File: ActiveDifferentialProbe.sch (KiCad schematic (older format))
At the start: 46 parts, among them J1 Conn_01x01, J16 Conn_01x01, J18 Conn_01x01, J19 Conn_01x01, J2 Conn_01x01, J20 Conn_01x01, J21 Conn_01x01, J22 Conn_01x01, J23 Conn_01x01, J25 Conn_Coaxial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

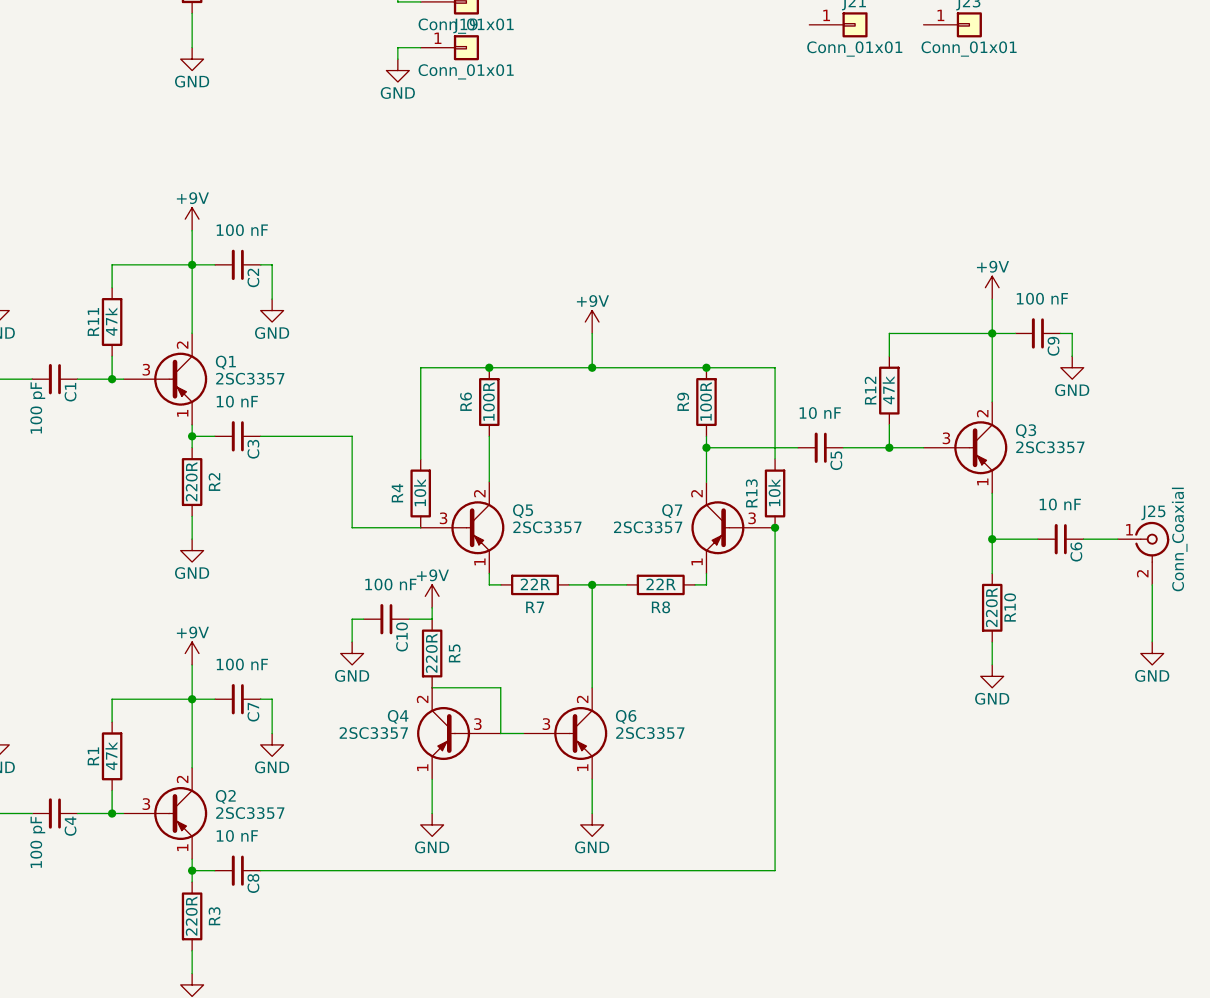
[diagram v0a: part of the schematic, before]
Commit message: Added LCSC parts, fixed symbol, added decoupling resistors
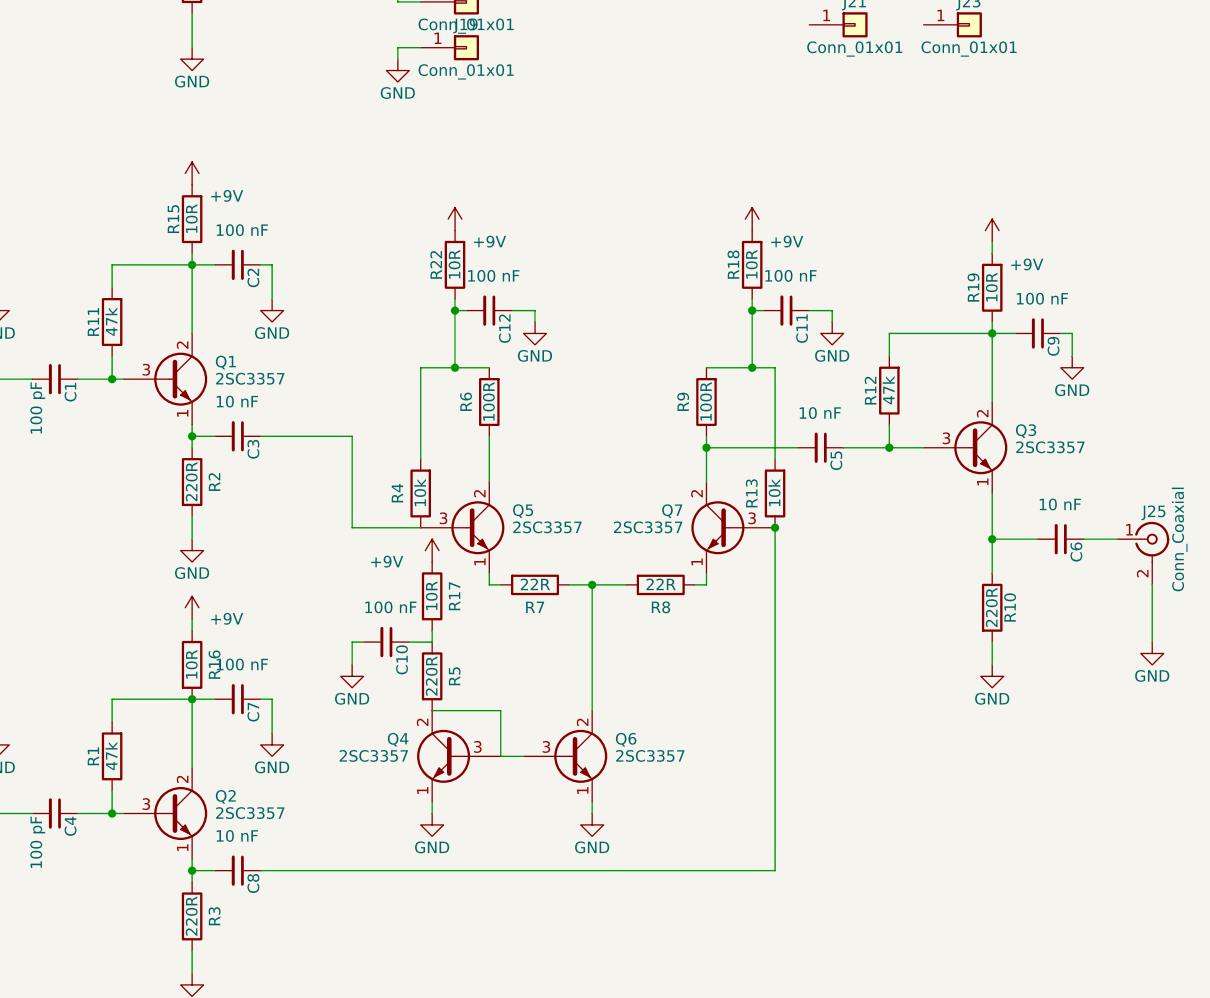
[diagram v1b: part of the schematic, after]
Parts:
- removed Q1, Q2, Q3, Q4, Q5, Q6, Q7: 2SC3357, TO_SOT_Packages_SMD:SOT-89-3_Handsoldering, symbol 2SA1015
- added C11, C12: 100 nF, Capacitors_SMD:C_0805_HandSoldering, symbol C_Small
- added Q1, Q2, Q3, Q4, Q5, Q6, Q7: 2SC3357, TO_SOT_Packages_SMD:SOT-89-3_Handsoldering, symbol 2SC1815
- added R15, R16, R17, R18, R19, R22: 10R, Resistors_SMD:R_0805_HandSoldering, symbol R
- C1, C4: LCSC (none) -> C1790
- C10, C2, C7, C9: LCSC (none) -> C49678
- C16: footprint Capacitors_SMD:C_1210_HandSoldering -> Capacitors_SMD:C_0805_HandSoldering; LCSC (none) -> C45783
- C3, C5, C6, C8: LCSC (none) -> C1710
- D6: LCSC (none) -> C2296
- R1, R11, R12: LCSC (none) -> C17713
- R10, R2, R3, R5: LCSC (none) -> C17557
- R13, R4: LCSC (none) -> C17414
- R14: LCSC (none) -> C17513
- R6, R9: LCSC (none) -> C17408
- R7, R8: LCSC (none) -> C17561
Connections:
- net +9V: now also R15.2, R16.1, R17.1, R18.2, R19.2, R22.2; no longer C10.1, C2.2, C7.2, C9.2, R1.2, R11.2, R12.2, R13.2, R4.2, R5.1, R6.2, R9.2
- net GND: now also C11.1, C12.1, Q4.1 (E), Q6.1 (E)
- net at C1.1, R11.1: now also Q1.3 (B)
- net at C3.2, R2.1: now also Q1.1 (E)
- net at C3.1, R4.1: now also Q5.3 (B)
- net at C5.1, R12.1: now also Q3.3 (B)
- net at C5.2, R9.1: now also Q7.2 (C)
- net at C6.2, R10.1: now also Q3.1 (E)
- net at C4.1, R1.1: now also Q2.3 (B)
- net at C8.2, R3.1: now also Q2.1 (E)
- net at C8.1, R13.1: now also Q7.3 (B)
- net at R5.2: now also Q4.2 (C), Q4.3 (B), Q6.3 (B)
- net at R7.1, R8.2: now also Q6.2 (C)
- net at R7.2: now also Q5.1 (E)
- net at R6.1: now also Q5.2 (C)
- net at R8.1: now also Q7.1 (E)
- new net: C2.2, Q1.2 (C), R11.2, R15.1
- new net: C9.2, Q3.2 (C), R12.2, R19.1
- new net: C7.2, Q2.2 (C), R1.2, R16.2
- new net: C10.1, R17.2, R5.1
- new net: C12.2, R22.1, R4.2, R6.2
- new net: C11.2, R13.2, R18.1, R9.2
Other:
- moved on the sheet: C10, R5

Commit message: Changed to 2SC3356
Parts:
- removed Q1, Q2, Q3, Q4, Q5, Q6, Q7: 2SC3357, TO_SOT_Packages_SMD:SOT-89-3_Handsoldering, symbol 2SC1815
- added Q1, Q2, Q3, Q4, Q5, Q6, Q7: 2SC3356, TO_SOT_Packages_SMD:SOT-23, symbol MMBT3904
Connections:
- net GND: now also Q4.2 (E), Q6.2 (E)
- net at C1.1, R11.1: now also Q1.1 (B)
- net at C3.2, R2.1: now also Q1.2 (E)
- net at C3.1, R4.1: now also Q5.1 (B)
- net at C5.1, R12.1: now also Q3.1 (B)
- net at C5.2, R9.1: now also Q7.3 (C)
- net at C6.2, R10.1: now also Q3.2 (E)
- net at C2.2, R11.2, R15.1: now also Q1.3 (C)
- net at C9.2, R12.2, R19.1: now also Q3.3 (C)
- net at C4.1, R1.1: now also Q2.1 (B)
- net at C8.2, R3.1: now also Q2.2 (E)
- net at C8.1, R13.1: now also Q7.1 (B)
- net at C7.2, R1.2, R16.2: now also Q2.3 (C)
- net at R5.2: now also Q4.1 (B), Q4.3 (C), Q6.1 (B)
- net at R7.1, R8.2: now also Q6.3 (C)
- net at R7.2: now also Q5.2 (E)
- net at R8.1: now also Q7.2 (E)
- net at R6.1: now also Q5.3 (C)

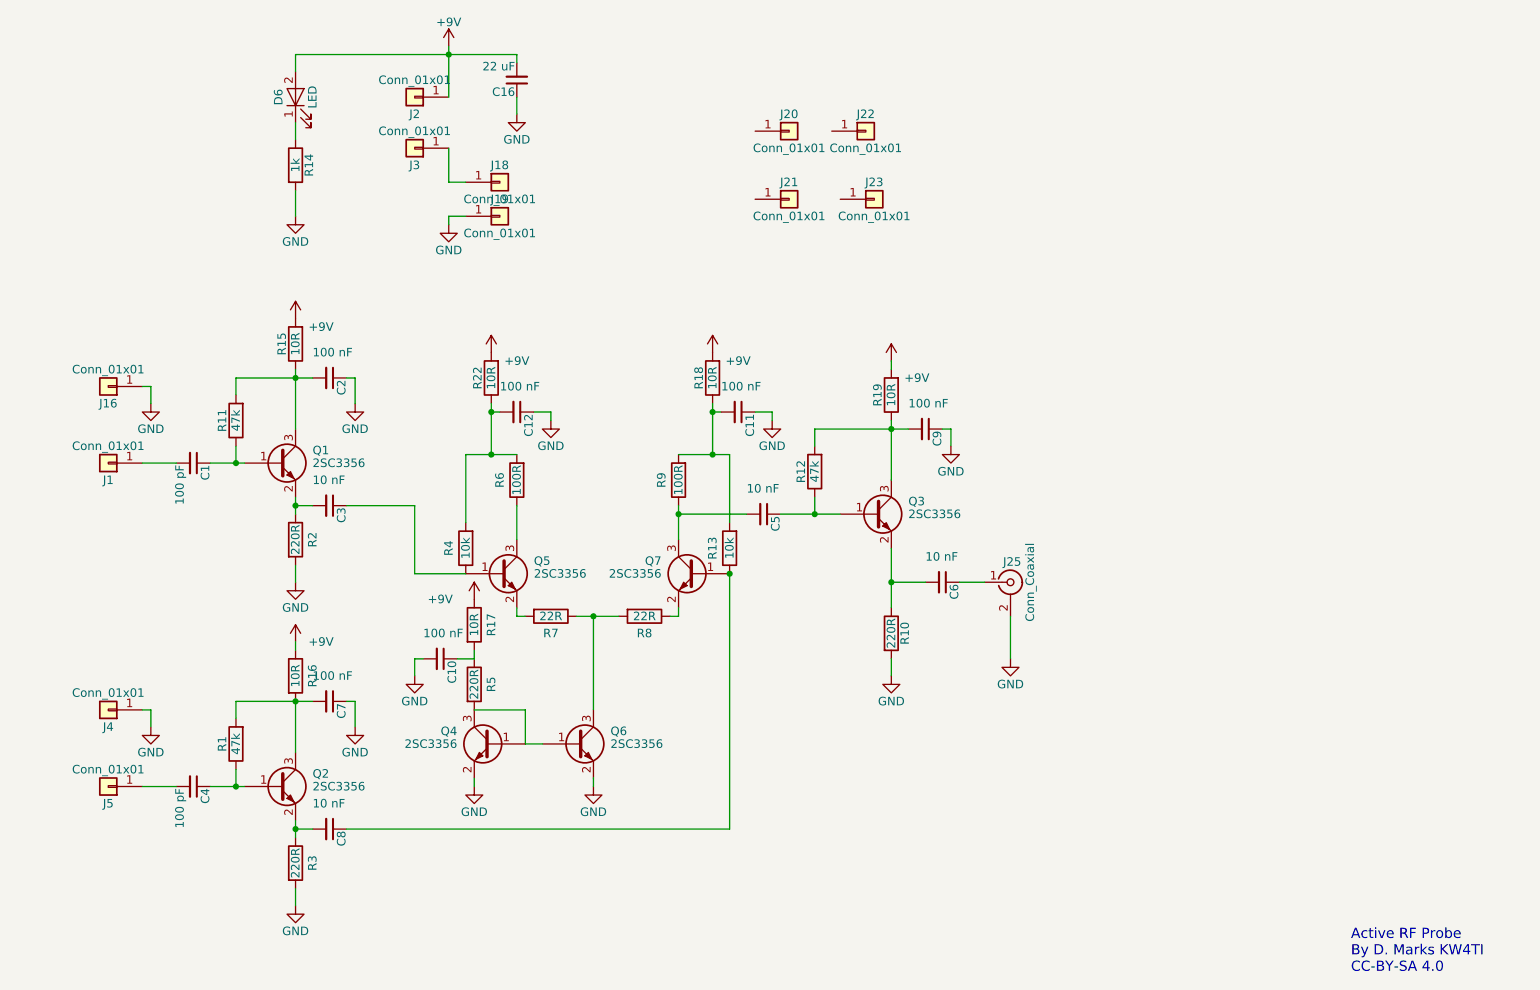
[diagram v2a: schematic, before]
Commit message: Added LCSC part numbers, added cutout notched, added series base resistors to emitter followers
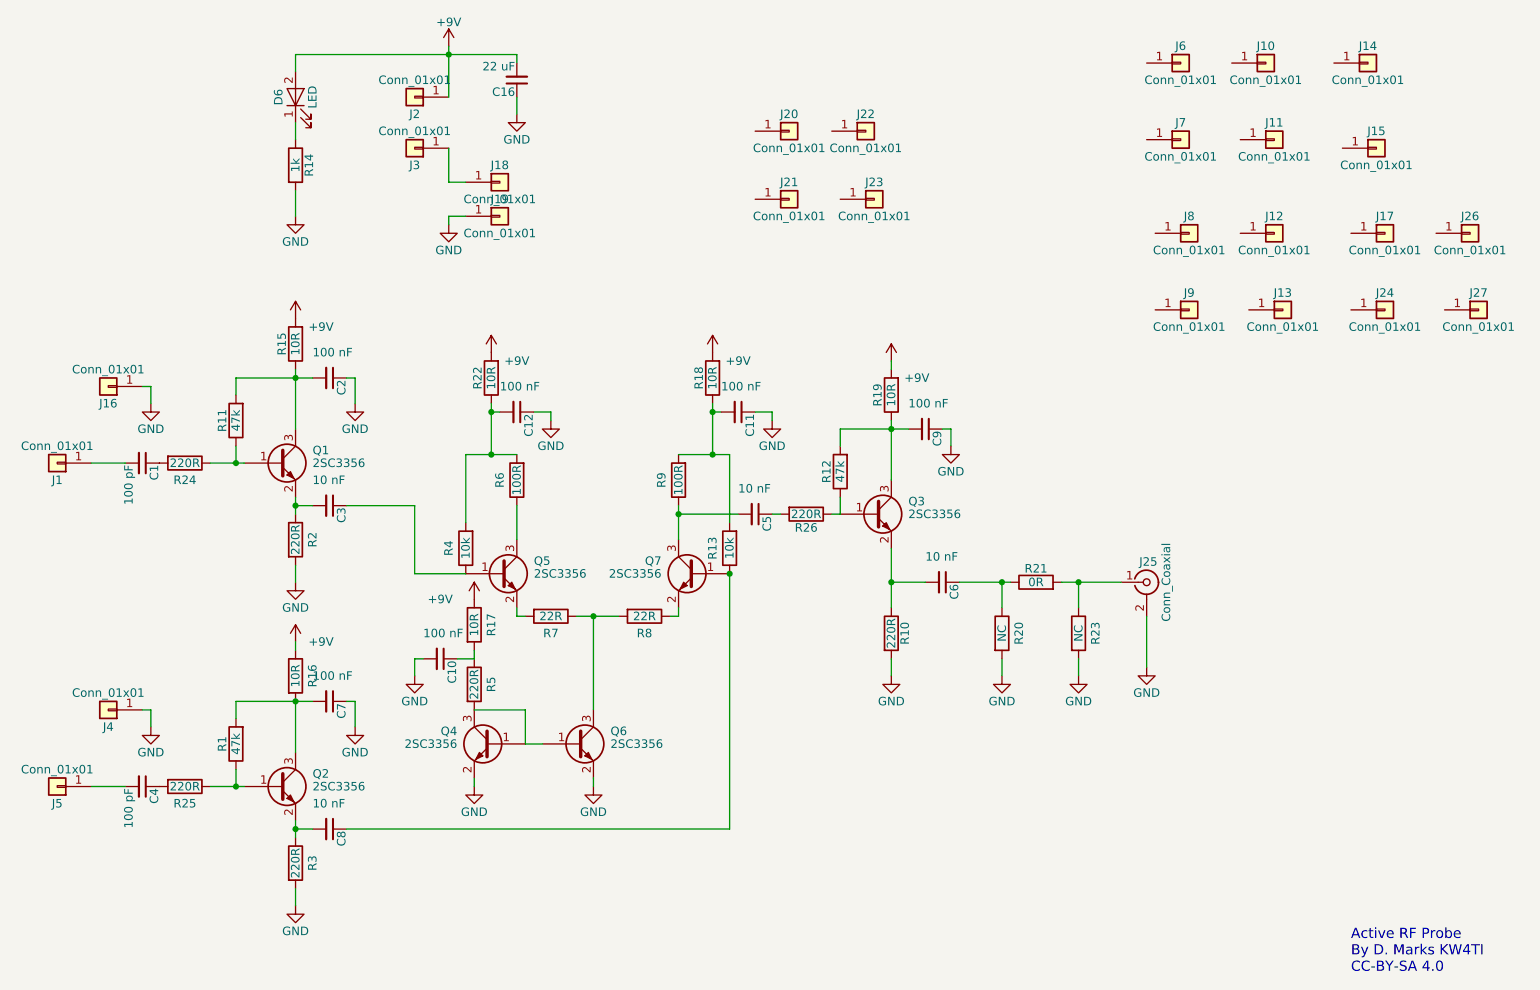
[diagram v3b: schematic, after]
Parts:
- added J10, J11, J12, J13, J14, J15, J17, J24, J26, J27, J6, J7, J8, J9: Conn_01x01, ActiveDifferentialProbe:BigSlot, symbol Conn_01x01
- added R20, R23: NC, Resistors_SMD:R_0805_HandSoldering, symbol R
- added R21: 0R, Resistors_SMD:R_0805_HandSoldering, symbol R
- added R24, R25, R26: 220R, Resistors_SMD:R_0805_HandSoldering, symbol R
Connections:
- net GND: now also R20.2, R23.2
- net at Q1.1 (B), R11.1: now also R24.1; no longer C1.1
- net at Q3.1 (B), R12.1: now also R26.1; no longer C5.1
- net at C6.1: now also R20.1, R21.1; no longer J25.1 (In)
- net at Q2.1 (B), R1.1: now also R25.1; no longer C4.1
- new net: C1.1, R24.2
- new net: C5.1, R26.2
- new net: J25.1 (In), R21.2, R23.1
- new net: C4.1, R25.2
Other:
- moved on the sheet: C1, C4, C5, J1, J25, J5, R12
